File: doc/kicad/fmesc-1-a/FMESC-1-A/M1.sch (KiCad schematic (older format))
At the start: 20 parts, among them Q1 AON6504, Q2 AON6504, Q3 AON6504, Q4 AON6504, Q5 AON6504, Q6 AON6504, U1 FD6288Q

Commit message: doc/kicad: FMESC-1-A  add DFN5x6_8L_EP1_P.kicad_mod
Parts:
- added JB1, JB2, JB3, JMA1, JMB1, JMC1: Conn_01x01, fmlibf:JS4x5mm, symbol Connector_Generic:Conn_01x01
- C10, C11, C12, C13: footprint (none) -> Capacitor_SMD:C_1206_3216Metric
- D11, D12, D13: footprint (none) -> Diode_SMD:D_SMA
- R11, R12, R13, R14, R15, R16: footprint (none) -> Resistor_SMD:R_0402_1005Metric
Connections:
- net A1: now also JMA1.1 (Pin_1)
- net B1: now also JMB1.1 (Pin_1)
- net C1: now also JMC1.1 (Pin_1)
- net VBAT: now also JB1.1 (Pin_1), JB2.1 (Pin_1), JB3.1 (Pin_1)

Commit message: doc/kicad: FMESC-1-A  add PCB
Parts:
- Q1, Q2, Q3, Q4, Q5, Q6: footprint (none) -> fmlibf:DFN5x6_8L_EP1_P
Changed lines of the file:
@@
 $Descr A4 11693 8268
 encoding utf-8
-Sheet 5 5
+Sheet 2 5
 Title "FMESC-1-A  M1"
 Date "2020-11-05"
@@
 AR Path="/5FA3EBFA/5FA18782" Ref="Q13"  Part="1"
 AR Path="/5FA3F05C/5FA18782" Ref="Q19"  Part="1"
-F 0 "Q19" H 2604 5546 50  0000 L CNN
+F 0 "Q1" H 2604 5546 50  0000 L CNN
 F 1 "AON6504" H 2604 5455 50  0000 L CNN
-F 2 "" H 2600 5600 50  0001 C CNN
+F 2 "fmlibf:DFN5x6_8L_EP1_P" H 2600 5600 50  0001 C CNN
 F 3 "~" H 2400 5500 50  0001 C CNN
 	1    2400 5500
@@
 AR Path="/5FA3EBFA/5FA18C7A" Ref="#PWR0111"  Part="1"
 AR Path="/5FA3F05C/5FA18C7A" Ref="#PWR0115"  Part="1"
-F 0 "#PWR0115" H 2500 5750 50  0001 C CNN
+F 0 "#PWR0103" H 2500 5750 50  0001 C CNN
 F 1 "GND" H 2505 5827 50  0000 C CNN
 F 2 "" H 2500 6000 50  0001 C CNN
@@
 AR Path="/5FA3EBFA/5FA18E6D" Ref="Q14"  Part="1"
 AR Path="/5FA3F05C/5FA18E6D" Ref="Q20"  Part="1"
-F 0 "Q20" H 2604 5046 50  0000 L CNN
+F 0 "Q2" H 2604 5046 50  0000 L CNN
 F 1 "AON6504" H 2604 4955 50  0000 L CNN
-F 2 "" H 2600 5100 50  0001 C CNN
+F 2 "fmlibf:DFN5x6_8L_EP1_P" H 2600 5100 50  0001 C CNN
 F 3 "~" H 2400 5000 50  0001 C CNN
 	1    2400 5000
@@
 AR Path="/5FA3EBFA/5FA19A2B" Ref="R32"  Part="1"
 AR Path="/5FA3F05C/5FA19A2B" Ref="R42"  Part="1"
-F 0 "R42" V 1843 5000 50  0000 C CNN
+F 0 "R12" V 1843 5000 50  0000 C CNN
 F 1 "10" V 1934 5000 50  0000 C CNN
 F 2 "Resistor_SMD:R_0402_1005Metric" V 1980 5000 50  0001 C CNN
@@
 AR Path="/5FA3EBFA/5FA19D20" Ref="R31"  Part="1"
 AR Path="/5FA3F05C/5FA19D20" Ref="R41"  Part="1"
-F 0 "R41" V 1843 5500 50  0000 C CNN
+F 0 "R11" V 1843 5500 50  0000 C CNN
 F 1 "10" V 1934 5500 50  0000 C CNN
 F 2 "Resistor_SMD:R_0402_1005Metric" V 1980 5500 50  0001 C CNN
@@
 AR Path="/5FA3EBFA/5FA1E885" Ref="Q15"  Part="1"
 AR Path="/5FA3F05C/5FA1E885" Ref="Q21"  Part="1"
-F 0 "Q21" H 4604 5546 50  0000 L CNN
+F 0 "Q3" H 4604 5546 50  0000 L CNN
 F 1 "AON6504" H 4604 5455 50  0000 L CNN
-F 2 "" H 4600 5600 50  0001 C CNN
+F 2 "fmlibf:DFN5x6_8L_EP1_P" H 4600 5600 50  0001 C CNN
 F 3 "~" H 4400 5500 50  0001 C CNN
 	1    4400 5500
@@
 AR Path="/5FA3EBFA/5FA1E88B" Ref="#PWR0112"  Part="1"
 AR Path="/5FA3F05C/5FA1E88B" Ref="#PWR0116"  Part="1"
-F 0 "#PWR0116" H 4500 5750 50  0001 C CNN
+F 0 "#PWR0104" H 4500 5750 50  0001 C CNN
 F 1 "GND" H 4505 5827 50  0000 C CNN
 F 2 "" H 4500 6000 50  0001 C CNN
@@
 AR Path="/5FA3EBFA/5FA1E892" Ref="Q16"  Part="1"
 AR Path="/5FA3F05C/5FA1E892" Ref="Q22"  Part="1"
-F 0 "Q22" H 4604 5046 50  0000 L CNN
+F 0 "Q4" H 4604 5046 50  0000 L CNN
 F 1 "AON6504" H 4604 4955 50  0000 L CNN
-F 2 "" H 4600 5100 50  0001 C CNN
+F 2 "fmlibf:DFN5x6_8L_EP1_P" H 4600 5100 50  0001 C CNN
 F 3 "~" H 4400 5000 50  0001 C CNN
 	1    4400 5000
@@
 AR Path="/5FA3EBFA/5FA1E8A1" Ref="R34"  Part="1"
 AR Path="/5FA3F05C/5FA1E8A1" Ref="R44"  Part="1"
-F 0 "R44" V 3843 5000 50  0000 C CNN
+F 0 "R14" V 3843 5000 50  0000 C CNN
 F 1 "10" V 3934 5000 50  0000 C CNN
 F 2 "Resistor_SMD:R_0402_1005Metric" V 3980 5000 50  0001 C CNN
@@
 AR Path="/5FA3EBFA/5FA1E8A7" Ref="R33"  Part="1"
 AR Path="/5FA3F05C/5FA1E8A7" Ref="R43"  Part="1"
-F 0 "R43" V 3843 5500 50  0000 C CNN
+F 0 "R13" V 3843 5500 50  0000 C CNN
 F 1 "10" V 3934 5500 50  0000 C CNN
 F 2 "Resistor_SMD:R_0402_1005Metric" V 3980 5500 50  0001 C CNN
@@
 AR Path="/5FA3EBFA/5FA23579" Ref="Q17"  Part="1"
 AR Path="/5FA3F05C/5FA23579" Ref="Q23"  Part="1"
-F 0 "Q23" H 6604 5546 50  0000 L CNN
+F 0 "Q5" H 6604 5546 50  0000 L CNN
 F 1 "AON6504" H 6604 5455 50  0000 L CNN
-F 2 "" H 6600 5600 50  0001 C CNN
+F 2 "fmlibf:DFN5x6_8L_EP1_P" H 6600 5600 50  0001 C CNN
 F 3 "~" H 6400 5500 50  0001 C CNN
 	1    6400 5500
@@
 AR Path="/5FA3EBFA/5FA2357F" Ref="#PWR0113"  Part="1"
 AR Path="/5FA3F05C/5FA2357F" Ref="#PWR0117"  Part="1"
-F 0 "#PWR0117" H 6500 5750 50  0001 C CNN
+F 0 "#PWR0105" H 6500 5750 50  0001 C CNN
 F 1 "GND" H 6505 5827 50  0000 C CNN
 F 2 "" H 6500 6000 50  0001 C CNN
@@
 AR Path="/5FA3EBFA/5FA23586" Ref="Q18"  Part="1"
 AR Path="/5FA3F05C/5FA23586" Ref="Q24"  Part="1"
-F 0 "Q24" H 6604 5046 50  0000 L CNN
+F 0 "Q6" H 6604 5046 50  0000 L CNN
 F 1 "AON6504" H 6604 4955 50  0000 L CNN
-F 2 "" H 6600 5100 50  0001 C CNN
+F 2 "fmlibf:DFN5x6_8L_EP1_P" H 6600 5100 50  0001 C CNN
 F 3 "~" H 6400 5000 50  0001 C CNN
 	1    6400 5000
@@
 AR Path="/5FA3EBFA/5FA23595" Ref="R36"  Part="1"
 AR Path="/5FA3F05C/5FA23595" Ref="R46"  Part="1"
-F 0 "R46" V 5843 5000 50  0000 C CNN
+F 0 "R16" V 5843 5000 50  0000 C CNN
 F 1 "10" V 5934 5000 50  0000 C CNN
 F 2 "Resistor_SMD:R_0402_1005Metric" V 5980 5000 50  0001 C CNN
@@
 AR Path="/5FA3EBFA/5FA2359B" Ref="R35"  Part="1"
 AR Path="/5FA3F05C/5FA2359B" Ref="R45"  Part="1"
-F 0 "R45" V 5843 5500 50  0000 C CNN
+F 0 "R15" V 5843 5500 50  0000 C CNN
 F 1 "10" V 5934 5500 50  0000 C CNN
 F 2 "Resistor_SMD:R_0402_1005Metric" V 5980 5500 50  0001 C CNN
@@
 AR Path="/5FA3EBFA/5FA29EC3" Ref="U3"  Part="1"
 AR Path="/5FA3F05C/5FA29EC3" Ref="U4"  Part="1"
-F 0 "U4" H 2950 2550 50  0000 L CNN
+F 0 "U1" H 2950 2550 50  0000 L CNN
 F 1 "FD6288Q" H 2850 2300 50  0000 L CNN
 F 2 "Package_DFN_QFN:QFN-24-1EP_4x4mm_P0.5mm_EP2.7x2.7mm" H 3000 1650 50  0001 C CNN
@@
 AR Path="/5FA3EBFA/5FA2C839" Ref="C30"  Part="1"
 AR Path="/5FA3F05C/5FA2C839" Ref="C40"  Part="1"
-F 0 "C40" H 1886 2654 50  0000 R CNN
+F 0 "C10" H 1886 2654 50  0000 R CNN
 F 1 "10u" H 1886 2745 50  0000 R CNN
 F 2 "Capacitor_SMD:C_1206_3216Metric" H 2038 2550 50  0001 C CNN
@@
 AR Path="/5FA3EBFA/5FA2CAED" Ref="#PWR0114"  Part="1"
 AR Path="/5FA3F05C/5FA2CAED" Ref="#PWR0118"  Part="1"
-F 0 "#PWR0118" H 2000 2600 50  0001 C CNN
+F 0 "#PWR0106" H 2000 2600 50  0001 C CNN
 F 1 "GND" H 2005 2677 50  0000 C CNN
 F 2 "" H 2000 2850 50  0001 C CNN
@@
 AR Path="/5FA3EBFA/5FA3A62C" Ref="C31"  Part="1"
 AR Path="/5FA3F05C/5FA3A62C" Ref="C41"  Part="1"
-F 0 "C41" H 4115 1546 50  0000 L CNN
+F 0 "C11" H 4115 1546 50  0000 L CNN
 F 1 "10u" H 4115 1455 50  0000 L CNN
 F 2 "Capacitor_SMD:C_1206_3216Metric" H 4038 1350 50  0001 C CNN
@@
 AR Path="/5FA3EBFA/5FA3A772" Ref="C32"  Part="1"
 AR Path="/5FA3F05C/5FA3A772" Ref="C42"  Part="1"
-F 0 "C42" H 4615 1546 50  0000 L CNN
+F 0 "C12" H 4615 1546 50  0000 L CNN
 F 1 "10u" H 4615 1455 50  0000 L CNN
 F 2 "Capacitor_SMD:C_1206_3216Metric" H 4538 1350 50  0001 C CNN
@@
 AR Path="/5FA3EBFA/5FA3A93C" Ref="C33"  Part="1"
 AR Path="/5FA3F05C/5FA3A93C" Ref="C43"  Part="1"
-F 0 "C43" H 5115 1546 50  0000 L CNN
+F 0 "C13" H 5115 1546 50  0000 L CNN
 F 1 "10u" H 5115 1455 50  0000 L CNN
 F 2 "Capacitor_SMD:C_1206_3216Metric" H 5038 1350 50  0001 C CNN
@@
 AR Path="/5FA3EBFA/5FA3AFB6" Ref="D31"  Part="1"
 AR Path="/5FA3F05C/5FA3AFB6" Ref="D41"  Part="1"
-F 0 "D41" V 4046 1120 50  0000 R CNN
+F 0 "D11" V 4046 1120 50  0000 R CNN
 F 1 "D" V 3955 1120 50  0000 R CNN
 F 2 "Diode_SMD:D_SMA" H 4000 1200 50  0001 C CNN
@@
 AR Path="/5FA3EBFA/5FA3B46A" Ref="D32"  Part="1"
 AR Path="/5FA3F05C/5FA3B46A" Ref="D42"  Part="1"
-F 0 "D42" V 4546 1120 50  0000 R CNN
+F 0 "D12" V 4546 1120 50  0000 R CNN
 F 1 "D" V 4455 1120 50  0000 R CNN
 F 2 "Diode_SMD:D_SMA" H 4500 1200 50  0001 C CNN
@@
 AR Path="/5FA3EBFA/5FA3B6F1" Ref="D33"  Part="1"
 AR Path="/5FA3F05C/5FA3B6F1" Ref="D43"  Part="1"
-F 0 "D43" V 5046 1120 50  0000 R CNN
+F 0 "D13" V 5046 1120 50  0000 R CNN
 F 1 "D" V 4955 1120 50  0000 R CNN
 F 2 "Diode_SMD:D_SMA" H 5000 1200 50  0001 C CNN
@@
 AR Path="/5FA3EBFA/5FA4238A" Ref="JB7"  Part="1"
 AR Path="/5FA3F05C/5FA4238A" Ref="JB10"  Part="1"
-F 0 "JB10" V 2464 4412 50  0000 R CNN
+F 0 "JB1" V 2464 4412 50  0000 R CNN
 F 1 "Conn_01x01" V 2373 4412 50  0000 R CNN
 F 2 "fmlibf:JS4x5mm" H 2500 4500 50  0001 C CNN
@@
 AR Path="/5FA3EBFA/5FA426D1" Ref="JB8"  Part="1"
 AR Path="/5FA3F05C/5FA426D1" Ref="JB11"  Part="1"
-F 0 "JB11" V 4464 4412 50  0000 R CNN
+F 0 "JB2" V 4464 4412 50  0000 R CNN
 F 1 "Conn_01x01" V 4373 4412 50  0000 R CNN
 F 2 "fmlibf:JS4x5mm" H 4500 4500 50  0001 C CNN
@@
 AR Path="/5FA3EBFA/5FA42AF1" Ref="JB9"  Part="1"
 AR Path="/5FA3F05C/5FA42AF1" Ref="JB12"  Part="1"
-F 0 "JB12" V 6464 4412 50  0000 R CNN
+F 0 "JB3" V 6464 4412 50  0000 R CNN
 F 1 "Conn_01x01" V 6373 4412 50  0000 R CNN
 F 2 "fmlibf:JS4x5mm" H 6500 4500 50  0001 C CNN
@@
 AR Path="/5FA3EBFA/5FA44AA6" Ref="JMA3"  Part="1"
 AR Path="/5FA3F05C/5FA44AA6" Ref="JMA4"  Part="1"
-F 0 "JMA4" H 3080 5292 50  0000 L CNN
+F 0 "JMA1" H 3080 5292 50  0000 L CNN
 F 1 "Conn_01x01" H 3080 5201 50  0000 L CNN
 F 2 "fmlibf:JS4x5mm" H 3000 5250 50  0001 C CNN
@@
 AR Path="/5FA3EBFA/5FA44F40" Ref="JMB3"  Part="1"
 AR Path="/5FA3F05C/5FA44F40" Ref="JMB4"  Part="1"
-F 0 "JMB4" H 5080 5292 50  0000 L CNN
+F 0 "JMB1" H 5080 5292 50  0000 L CNN
 F 1 "Conn_01x01" H 5080 5201 50  0000 L CNN
 F 2 "fmlibf:JS4x5mm" H 5000 5250 50  0001 C CNN
@@
 AR Path="/5FA3EBFA/5FA4532B" Ref="JMC3"  Part="1"
 AR Path="/5FA3F05C/5FA4532B" Ref="JMC4"  Part="1"
-F 0 "JMC4" H 7080 5292 50  0000 L CNN
+F 0 "JMC1" H 7080 5292 50  0000 L CNN
 F 1 "Conn_01x01" H 7080 5201 50  0000 L CNN
 F 2 "fmlibf:JS4x5mm" H 7000 5250 50  0001 C CNN

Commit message: doc/kicad: FMESC-1-A  update PCB
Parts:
- added JG1, JG2, JG3: Conn_01x01, fmlibf:JS3x4mm, symbol Connector_Generic:Conn_01x01
- JB1, JB2, JB3: footprint fmlibf:JS4x5mm -> fmlibf:JS3x5mm
- MA1: renamed from JMA1; footprint fmlibf:JS4x5mm -> fmlibf:JS3x4mm
- MB1: renamed from JMB1; footprint fmlibf:JS4x5mm -> fmlibf:JS3x4mm
- MC1: renamed from JMC1; footprint fmlibf:JS4x5mm -> fmlibf:JS3x4mm
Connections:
- net GND: now also JG1.1 (Pin_1), JG2.1 (Pin_1), JG3.1 (Pin_1)
- net VBAT renamed +BATT

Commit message: doc/kicad: FMESC-1-A  PCB add wire (some)
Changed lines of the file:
@@
 AR Path="/5FA3EBFA/5FA18C7A" Ref="#PWR0111"  Part="1"
 AR Path="/5FA3F05C/5FA18C7A" Ref="#PWR0115"  Part="1"
-F 0 "#PWR0103" H 2500 5750 50  0001 C CNN
+F 0 "#PWR0115" H 2500 5750 50  0001 C CNN
 F 1 "GND" H 2505 5827 50  0000 C CNN
 F 2 "" H 2500 6000 50  0001 C CNN
@@
 AR Path="/5FA3EBFA/5FA1E88B" Ref="#PWR0112"  Part="1"
 AR Path="/5FA3F05C/5FA1E88B" Ref="#PWR0116"  Part="1"
-F 0 "#PWR0104" H 4500 5750 50  0001 C CNN
+F 0 "#PWR0116" H 4500 5750 50  0001 C CNN
 F 1 "GND" H 4505 5827 50  0000 C CNN
 F 2 "" H 4500 6000 50  0001 C CNN
@@
 AR Path="/5FA3EBFA/5FA2357F" Ref="#PWR0113"  Part="1"
 AR Path="/5FA3F05C/5FA2357F" Ref="#PWR0117"  Part="1"
-F 0 "#PWR0105" H 6500 5750 50  0001 C CNN
+F 0 "#PWR0117" H 6500 5750 50  0001 C CNN
 F 1 "GND" H 6505 5827 50  0000 C CNN
 F 2 "" H 6500 6000 50  0001 C CNN
@@
 AR Path="/5FA3EBFA/5FA2CAED" Ref="#PWR0114"  Part="1"
 AR Path="/5FA3F05C/5FA2CAED" Ref="#PWR0118"  Part="1"
-F 0 "#PWR0106" H 2000 2600 50  0001 C CNN
+F 0 "#PWR0118" H 2000 2600 50  0001 C CNN
 F 1 "GND" H 2005 2677 50  0000 C CNN
 F 2 "" H 2000 2850 50  0001 C CNN
@@
 Text Label 3250 3150 3    50   ~ 0
 C1
-Text Label 1500 1000 0    50   ~ 0
+Text Label 2000 1000 0    50   ~ 0
 VC
 Text Label 2000 2550 0    50   ~ 0
@@
 AR Path="/5FA3EBFA/5FA6301C" Ref="#PWR0125"  Part="1"
 AR Path="/5FA3F05C/5FA6301C" Ref="#PWR0128"  Part="1"
-F 0 "#PWR0119" H 2500 4350 50  0001 C CNN
+F 0 "#PWR0128" H 2500 4350 50  0001 C CNN
 F 1 "+BATT" H 2515 4673 50  0000 C CNN
 F 2 "" H 2500 4500 50  0001 C CNN
@@
 AR Path="/5FA3EBFA/5FA76D98" Ref="#PWR0126"  Part="1"
 AR Path="/5FA3F05C/5FA76D98" Ref="#PWR0129"  Part="1"
-F 0 "#PWR0120" H 4500 4350 50  0001 C CNN
+F 0 "#PWR0129" H 4500 4350 50  0001 C CNN
 F 1 "+BATT" H 4515 4673 50  0000 C CNN
 F 2 "" H 4500 4500 50  0001 C CNN
@@
 AR Path="/5FA3EBFA/5FA770E9" Ref="#PWR0127"  Part="1"
 AR Path="/5FA3F05C/5FA770E9" Ref="#PWR0130"  Part="1"
-F 0 "#PWR0121" H 6500 4350 50  0001 C CNN
+F 0 "#PWR0130" H 6500 4350 50  0001 C CNN
 F 1 "+BATT" H 6515 4673 50  0000 C CNN
 F 2 "" H 6500 4500 50  0001 C CNN
@@
 Wire Wire Line
 	6500 4600 6500 4800
+Wire Wire Line
+	1500 1000 2000 1000
 $EndSCHEMATC

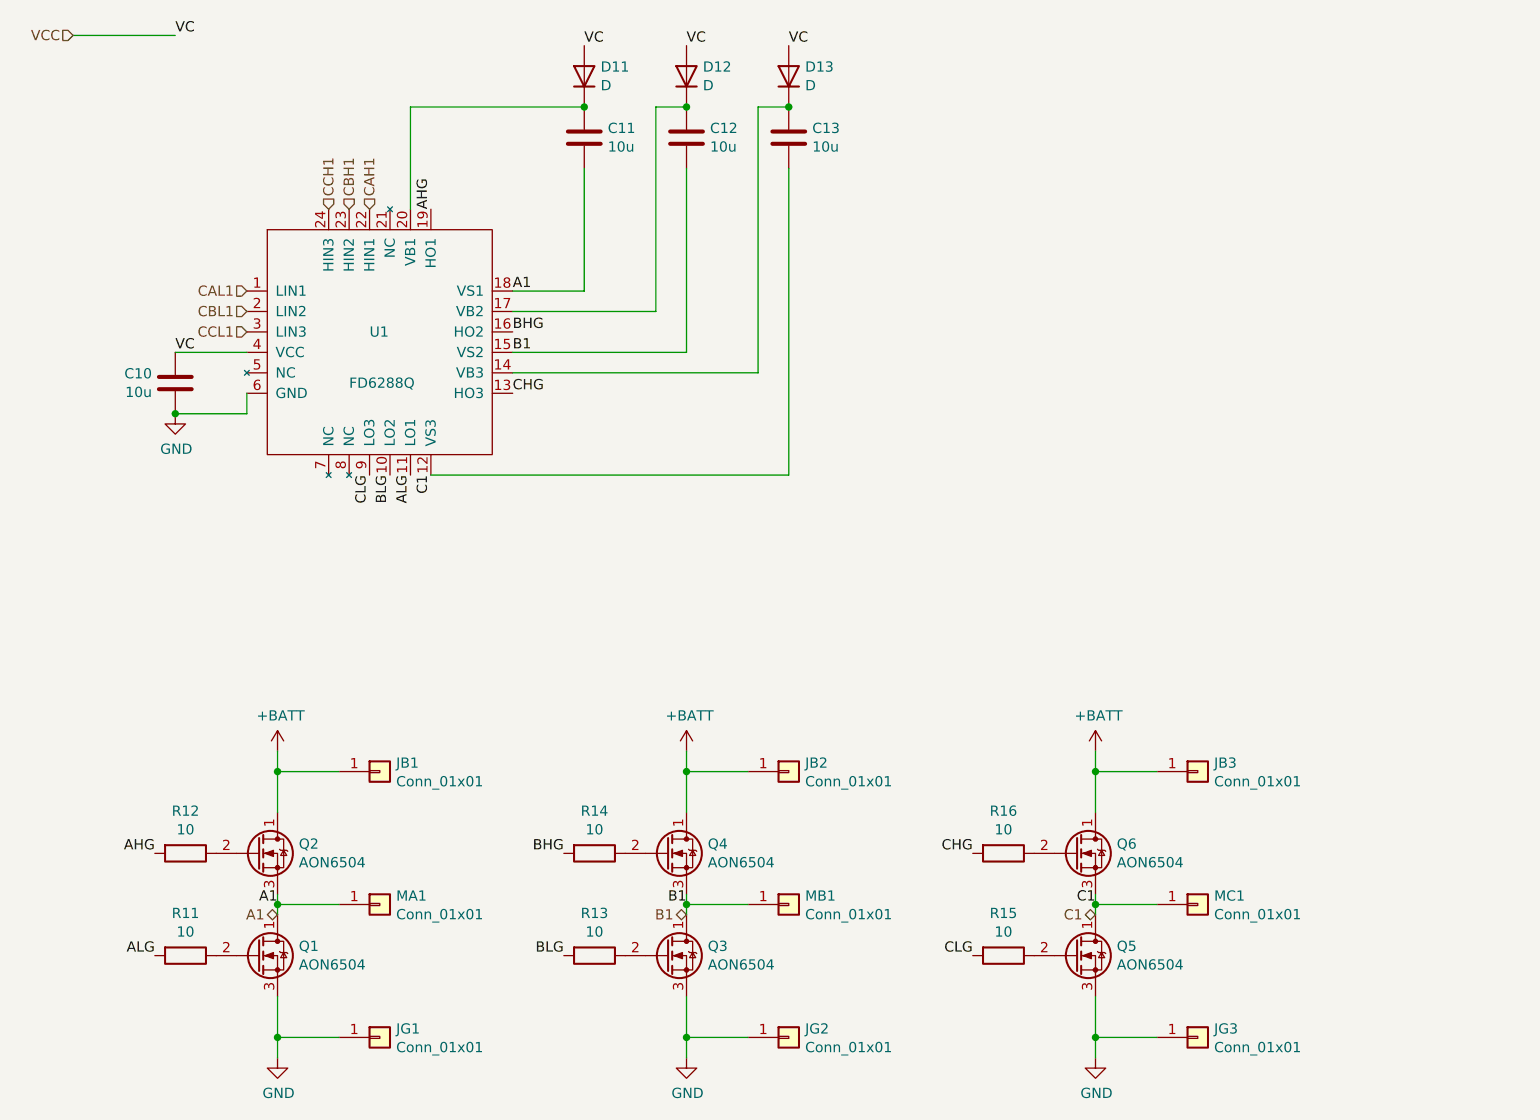
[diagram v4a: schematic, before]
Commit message: doc/kicad: add FMESC-1-C
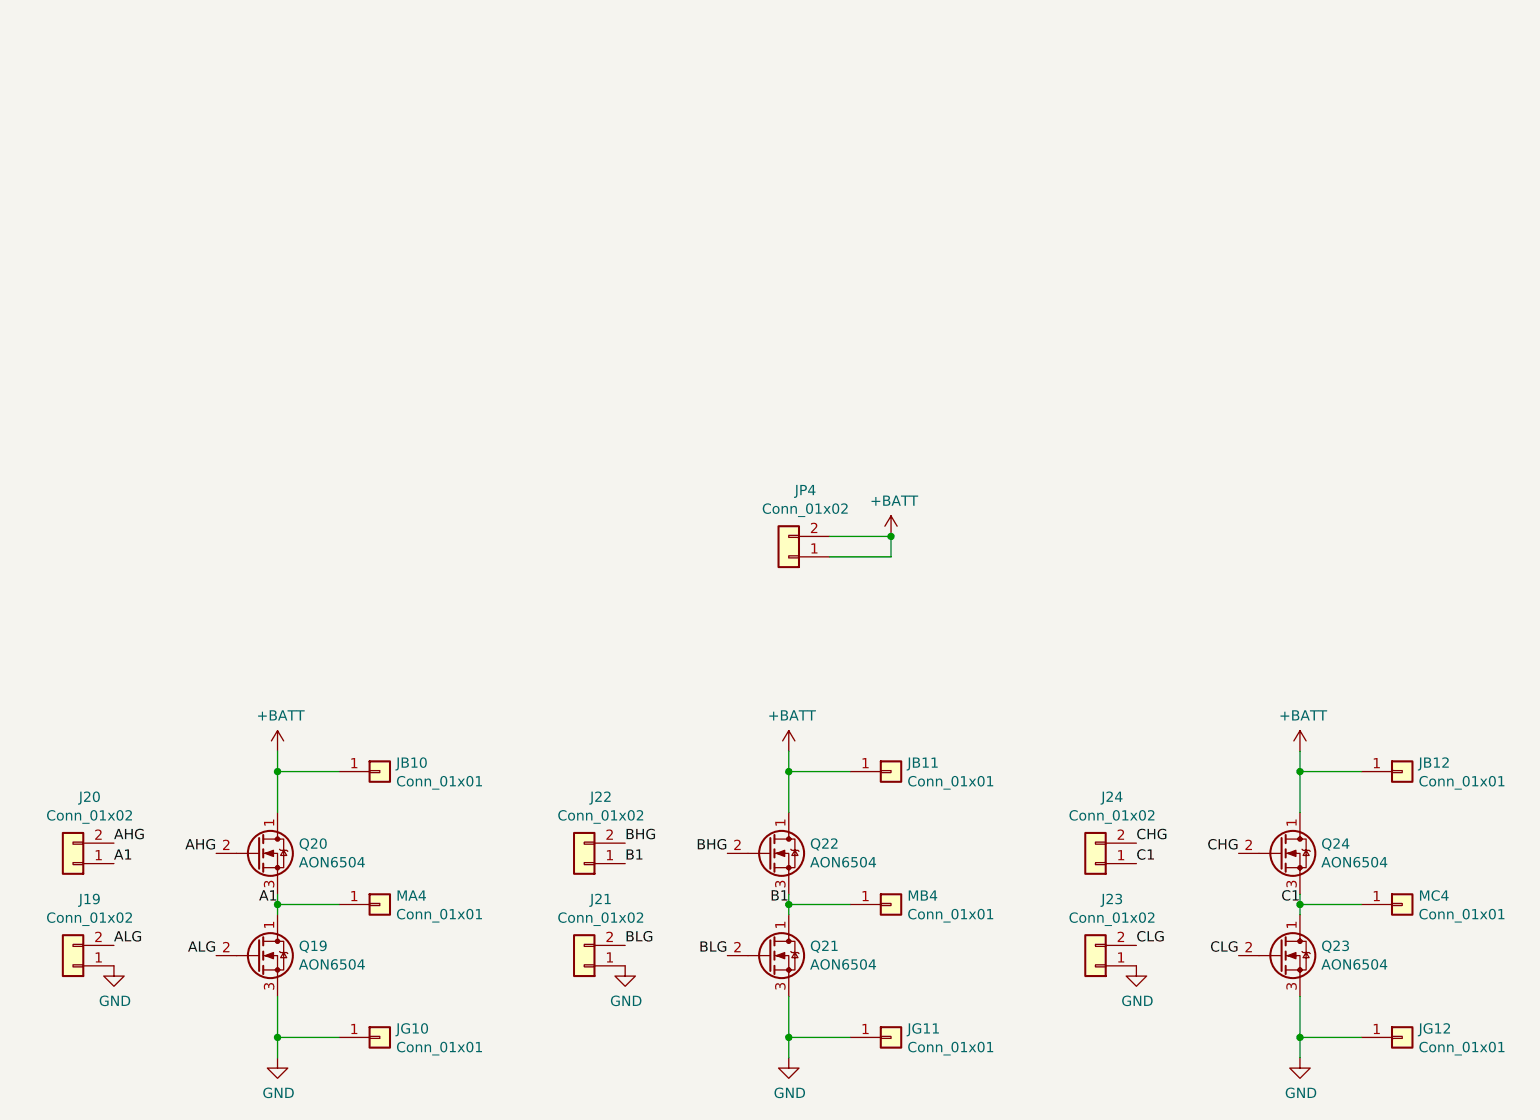
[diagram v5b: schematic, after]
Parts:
- removed C10, C11, C12, C13: 10u, Capacitor_SMD:C_1206_3216Metric, symbol Device:C
- removed D11, D12, D13: D, Diode_SMD:D_SMA, symbol Device:D
- removed R11, R12, R13, R14, R15, R16: 10, Resistor_SMD:R_0402_1005Metric, symbol Device:R
- removed U1: FD6288Q, Package_DFN_QFN:QFN-24-1EP_4x4mm_P0.5mm_EP2.7x2.7mm, symbol fmlibs:FD6288Q
- added J1, J2, J3, J4, J5, J6, JP1: Conn_01x02, symbol Connector_Generic:Conn_01x02
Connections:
- net +BATT: now also JP1.1 (Pin_1), JP1.2 (Pin_2)
- net A1: now also J2.1 (Pin_1)
- net AHG: now also Q2.2 (G), J2.2 (Pin_2)
- net ALG: now also Q1.2 (G), J1.2 (Pin_2)
- net B1: now also J4.1 (Pin_1)
- net BHG: now also Q4.2 (G), J4.2 (Pin_2)
- net BLG: now also Q3.2 (G), J3.2 (Pin_2)
- net C1: now also J6.1 (Pin_1)
- net CHG: now also Q6.2 (G), J6.2 (Pin_2)
- net CLG: now also Q5.2 (G), J5.2 (Pin_2)
- net GND: now also J1.1 (Pin_1), J3.1 (Pin_1), J5.1 (Pin_1)
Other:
- moved on the sheet: JB11, JB12, JG11, JG12, MB4, MC4, Q21, Q22, Q23, Q24

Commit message: doc/kicad: FMESC-1-A update PCB
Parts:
- J1, J2, J3, J4, J5, J6, JP1: footprint (none) -> fmlibf:JS_2P_1.0mm
- JG1, JG2, JG3, MA1, MB1, MC1: footprint fmlibf:JS3x4mm -> fmlibf:JS3x3.5mm

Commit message: doc/kicad: FMESC-1-A clean PCB
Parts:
- JG1, JG2, JG3: footprint fmlibf:JS3x3.5mm -> fmlibf:JS2x3.5mm
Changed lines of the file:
@@
 F 0 "JG1" H 3080 5942 50  0000 L CNN
 F 1 "Conn_01x01" H 3080 5851 50  0000 L CNN
-F 2 "fmlibf:JS3x3.5mm" H 3000 5900 50  0001 C CNN
+F 2 "fmlibf:JS2x3.5mm" H 3000 5900 50  0001 C CNN
 F 3 "~" H 3000 5900 50  0001 C CNN
 	1    3000 5900
@@
 F 0 "JG2" H 5580 5942 50  0000 L CNN
 F 1 "Conn_01x01" H 5580 5851 50  0000 L CNN
-F 2 "fmlibf:JS3x3.5mm" H 5500 5900 50  0001 C CNN
+F 2 "fmlibf:JS2x3.5mm" H 5500 5900 50  0001 C CNN
 F 3 "~" H 5500 5900 50  0001 C CNN
 	1    5500 5900
@@
 F 0 "JG3" H 8080 5942 50  0000 L CNN
 F 1 "Conn_01x01" H 8080 5851 50  0000 L CNN
-F 2 "fmlibf:JS3x3.5mm" H 8000 5900 50  0001 C CNN
+F 2 "fmlibf:JS2x3.5mm" H 8000 5900 50  0001 C CNN
 F 3 "~" H 8000 5900 50  0001 C CNN
 	1    8000 5900
